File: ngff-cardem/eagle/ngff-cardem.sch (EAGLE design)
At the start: 143 parts, among them IC201 CB3Q3244PW, IC202 CB3Q3244PW, IC203 IP4234CZ6, IC204 FPF2109, IC205 FPF2109, IC301 TPS22958N-DGN, IC302 TPS22958N-DGK, J301 PJ-002BH-SMT-TR, M2 MENTOR_12701001, M3 MENTOR_12701001, Q201 12MHz, T101 BC847, T102 BC847, U201 IP4234CZ6, U202 AT91SAM3S-AU, U301 MIC5366-1.8YC5, X101 PINHD-2X3-SP, X102 ZX360D-B-10P(30), X201 MINI-USB-SHIELD-UX60-MB-5ST, X202 2.54mm, X203 JACK2.5_SJ-2523, X301 171826-4-RA

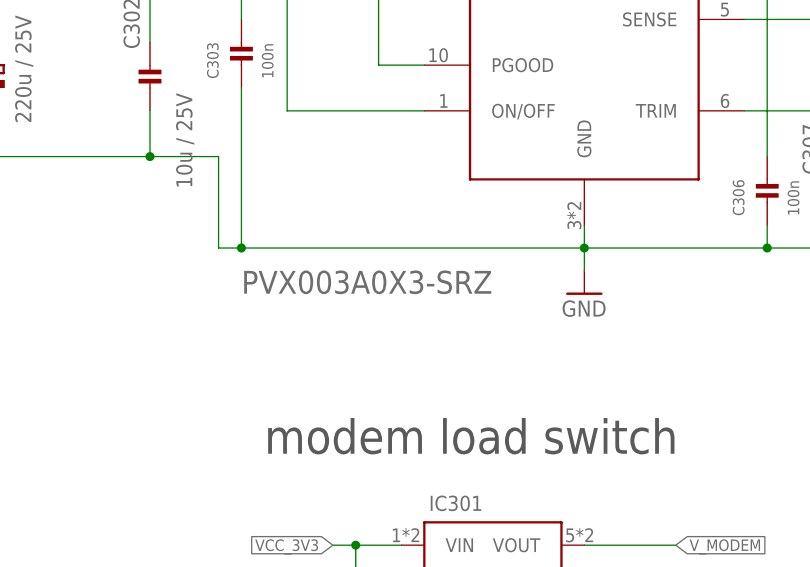
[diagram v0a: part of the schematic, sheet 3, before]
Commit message: ngff-cardem: make DCDC301 default to Murata OKL-T/3-W12P-C
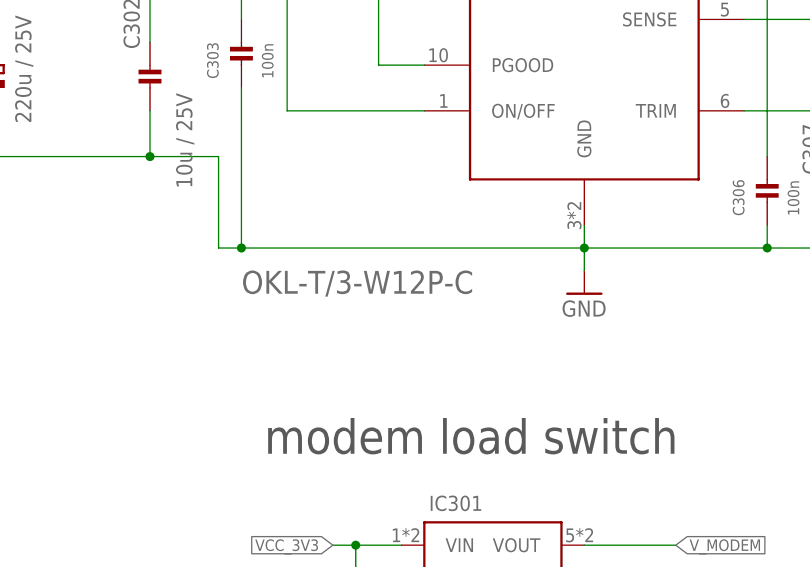
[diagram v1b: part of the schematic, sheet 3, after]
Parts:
- DCDC301: value PVX003A0X3-SRZ -> OKL-T/3-W12P-C; DESCRIPTION DC DC CONVERTER 0.6-5.5V 16.5W -> DC DC CONVERTER 0.591-5.5V 15W; LINK https://www.digikey.de/product-detail/de/abb-power-electron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 -> https://www.digikey.de/product-detail/de/murata-power-solut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; MANUFACTURER ABB Power Electronics Inc. -> Murata Power Solutions Inc.; MANUFACTURERPARTNUMBER PVX003A0X3-SRZ -> OKL-T/3-W12P-C; SOURCEPARTNUMBER 555-1264-1-ND -> 811-2709-1-ND
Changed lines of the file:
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@@
 <attribute name="SOURCEPARTNUMBER" value="732-6126-1-ND"/>
 </part>
-<part name="DCDC301" library="DC-DC_CONVERTER" deviceset="DCDC-GE-PVX" device="-ALL" value="PVX003A0X3-SRZ">
+<part name="DCDC301" library="DC-DC_CONVERTER" deviceset="DCDC-GE-PVX" device="-ALL" value="OKL-T/3-W12P-C">
 <attribute name="CLASS" value="DC/DC CONVERTER"/>
-<attribute name="DESCRIPTION" value="DC DC CONVERTER 0.6-5.5V 16.5W"/>
-<attribute name="LINK" value="https://www.digikey.de/product-detail/de/abb-power-electronics-inc/PVX003A0X3-SRZ/555-1264-1-ND"/>
-<attribute name="MANUFACTURER" value="ABB Power Electronics Inc."/>
-<attribute name="MANUFACTURERPARTNUMBER" value="PVX003A0X3-SRZ"/>
+<attribute name="DESCRIPTION" value="DC DC CONVERTER 0.591-5.5V 15W"/>
+<attribute name="LINK" value="https://www.digikey.de/product-detail/de/murata-power-solutions-inc/OKL-T-3-W12P-C/811-2709-1-ND"/>
+<attribute name="MANUFACTURER" value="Murata Power Solutions Inc."/>
+<attribute name="MANUFACTURERPARTNUMBER" value="OKL-T/3-W12P-C"/>
 <attribute name="POPULATED" value="TRUE"/>
 <attribute name="ROHSCERTIFICATE" value="RoHS-konform"/>
 <attribute name="SOURCE" value="DIGIKEY"/>
-<attribute name="SOURCEPARTNUMBER" value="555-1264-1-ND"/>
+<attribute name="SOURCEPARTNUMBER" value="811-2709-1-ND"/>
 </part>
 <part name="R304" library="rc-sysmocom" deviceset="RESISTOR" device="_0603" value="100k">
@@
 <attribute name="NAME" x="273.558" y="252.73" size="2.54" layer="95"/>
 <attribute name="VALUE" x="243.84" y="213.36" size="2.54" layer="96"/>
-<attribute name="DESCRIPTION" x="281.94" y="238.76" size="1.27" layer="96" display="off"/>
-<attribute name="MANUFACTURER" x="281.94" y="238.76" size="1.27" layer="96" display="off"/>
-<attribute name="MANUFACTURERPARTNUMBER" x="281.94" y="238.76" size="1.27" layer="96" display="off"/>
-<attribute name="SOURCE" x="281.94" y="238.76" size="1.27" layer="96" display="off"/>
-<attribute name="SOURCEPARTNUMBER" x="281.94" y="238.76" size="1.27" layer="96" display="off"/>
-<attribute name="ROHSCERTIFICATE" x="281.94" y="238.76" size="1.27" layer="96" display="off"/>
-<attribute name="POPULATED" x="281.94" y="238.76" size="1.27" layer="96" display="off"/>
-<attribute name="CLASS" x="281.94" y="238.76" size="1.27" layer="96" display="off"/>
-<attribute name="LINK" x="281.94" y="238.76" size="1.27" layer="96" display="off"/>
+<attribute name="DESCRIPTION" x="281.94" y="238.76" size="1.778" layer="96" display="off"/>
+<attribute name="MANUFACTURER" x="281.94" y="238.76" size="1.778" layer="96" display="off"/>
+<attribute name="MANUFACTURERPARTNUMBER" x="281.94" y="238.76" size="1.778" layer="96" display="off"/>
+<attribute name="SOURCE" x="281.94" y="238.76" size="1.778" layer="96" display="off"/>
+<attribute name="SOURCEPARTNUMBER" x="281.94" y="238.76" size="1.778" layer="96" display="off"/>
+<attribute name="ROHSCERTIFICATE" x="281.94" y="238.76" size="1.778" layer="96" display="off"/>
+<attribute name="POPULATED" x="281.94" y="238.76" size="1.778" layer="96" display="off"/>
+<attribute name="CLASS" x="281.94" y="238.76" size="1.778" layer="96" display="off"/>
+<attribute name="LINK" x="281.94" y="238.76" size="1.778" layer="96" display="off"/>
 </instance>
 <instance part="R304" gate="G$1" x="264.16" y="256.54" smashed="yes" rot="R180">

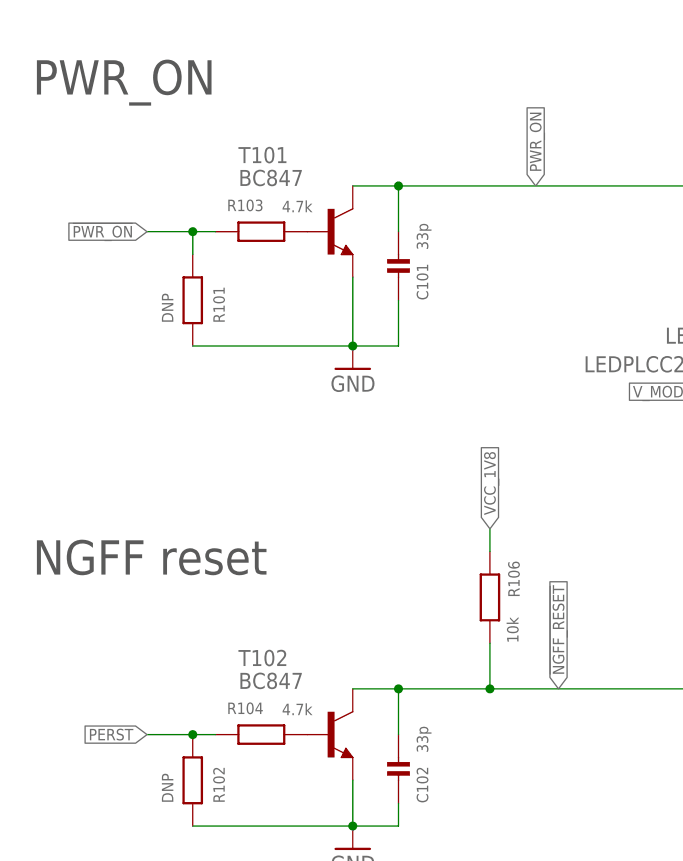
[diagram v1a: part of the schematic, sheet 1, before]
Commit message: ngff-cardem: exchange two BJT to available types (BC850)
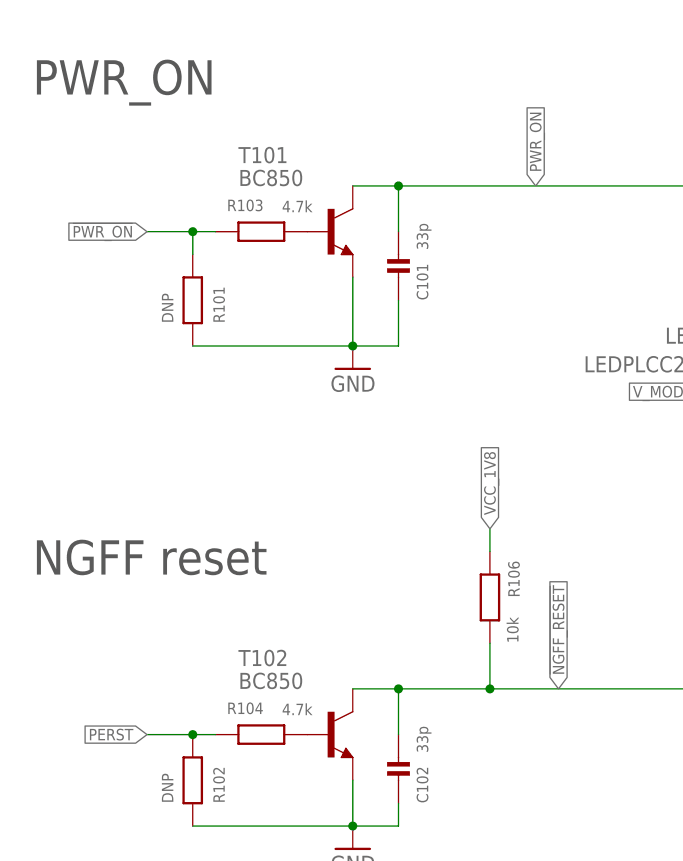
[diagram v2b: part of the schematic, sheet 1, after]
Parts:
- T101, T102: value BC847 -> BC850; DESCRIPTION TRANS NPN 45V 0.1A SOT23 -> TRANS NPN 45V 100MA TO236AB; LINK https://www.digikey.de/product-detail/de/nexperia-usa-inc/BC847C,215/1727-2924-1-ND -> https://www.digikey.de/product-detail/de/nexperia-usa-inc/BC850C-235/1727-6194-1-ND/; MANUFACTURERPARTNUMBER BC847C,215 -> BC850C,235; SOURCEPARTNUMBER 1727-2924-1-ND -> 1727-6194-1-ND
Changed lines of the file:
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@@
 <attribute name="SOURCEPARTNUMBER" value="A121523CT-ND"/>
 </part>
-<part name="T101" library="transistor" deviceset="*-NPN-" device="SOT23-BEC" technology="BC847C" value="BC847">
+<part name="T101" library="transistor" deviceset="*-NPN-" device="SOT23-BEC" technology="BC847C" value="BC850">
 <attribute name="CLASS" value="TRANSISTOR"/>
-<attribute name="DESCRIPTION" value="TRANS NPN 45V 0.1A SOT23"/>
-<attribute name="LINK" value="https://www.digikey.de/product-detail/de/nexperia-usa-inc/BC847C,215/1727-2924-1-ND"/>
+<attribute name="DESCRIPTION" value="TRANS NPN 45V 100MA TO236AB"/>
+<attribute name="LINK" value="https://www.digikey.de/product-detail/de/nexperia-usa-inc/BC850C-235/1727-6194-1-ND/"/>
 <attribute name="MANUFACTURER" value="Nexperia USA Inc."/>
-<attribute name="MANUFACTURERPARTNUMBER" value="BC847C,215"/>
-<attribute name="POPULATED" value="TRUE"/>
-<attribute name="ROHSCERTIFICATE" value="RoHS3-konform"/>
-<attribute name="SOURCE" value="DIGIKEY"/>
-<attribute name="SOURCEPARTNUMBER" value="1727-2924-1-ND"/>
+<attribute name="MANUFACTURERPARTNUMBER" value="BC850C,235"/>
+<attribute name="POPULATED" value="TRUE"/>
+<attribute name="ROHSCERTIFICATE" value="RoHS3-konform"/>
+<attribute name="SOURCE" value="DIGIKEY"/>
+<attribute name="SOURCEPARTNUMBER" value="1727-6194-1-ND"/>
 </part>
 <part name="GND47" library="supply1" deviceset="GND" device=""/>
@@
 <attribute name="SOURCEPARTNUMBER" value="A129611CT-ND"/>
 </part>
-<part name="T102" library="transistor" deviceset="*-NPN-" device="SOT23-BEC" technology="BC847C" value="BC847">
+<part name="T102" library="transistor" deviceset="*-NPN-" device="SOT23-BEC" technology="BC847C" value="BC850">
 <attribute name="CLASS" value="TRANSISTOR"/>
-<attribute name="DESCRIPTION" value="TRANS NPN 45V 0.1A SOT23"/>
-<attribute name="LINK" value="https://www.digikey.de/product-detail/de/nexperia-usa-inc/BC847C,215/1727-2924-1-ND"/>
+<attribute name="DESCRIPTION" value="TRANS NPN 45V 100MA TO236AB"/>
+<attribute name="LINK" value="https://www.digikey.de/product-detail/de/nexperia-usa-inc/BC850C-235/1727-6194-1-ND/"/>
 <attribute name="MANUFACTURER" value="Nexperia USA Inc."/>
-<attribute name="MANUFACTURERPARTNUMBER" value="BC847C,215"/>
-<attribute name="POPULATED" value="TRUE"/>
-<attribute name="ROHSCERTIFICATE" value="RoHS3-konform"/>
-<attribute name="SOURCE" value="DIGIKEY"/>
-<attribute name="SOURCEPARTNUMBER" value="1727-2924-1-ND"/>
+<attribute name="MANUFACTURERPARTNUMBER" value="BC850C,235"/>
+<attribute name="POPULATED" value="TRUE"/>
+<attribute name="ROHSCERTIFICATE" value="RoHS3-konform"/>
+<attribute name="SOURCE" value="DIGIKEY"/>
+<attribute name="SOURCEPARTNUMBER" value="1727-6194-1-ND"/>
 </part>
 <part name="GND16" library="supply1" deviceset="GND" device=""/>
@@
 </instance>
 <instance part="T101" gate="G$1" x="60.96" y="195.58">
-<attribute name="DESCRIPTION" x="60.96" y="195.58" size="1.778" layer="96" rot="MR0" display="off"/>
-<attribute name="MANUFACTURER" x="60.96" y="195.58" size="1.778" layer="96" rot="MR0" display="off"/>
-<attribute name="MANUFACTURERPARTNUMBER" x="60.96" y="195.58" size="1.778" layer="96" rot="MR0" display="off"/>
-<attribute name="SOURCE" x="60.96" y="195.58" size="1.778" layer="96" rot="MR0" display="off"/>
-<attribute name="SOURCEPARTNUMBER" x="60.96" y="195.58" size="1.778" layer="96" rot="MR0" display="off"/>
-<attribute name="ROHSCERTIFICATE" x="60.96" y="195.58" size="1.778" layer="96" rot="MR0" display="off"/>
-<attribute name="POPULATED" x="60.96" y="195.58" size="1.778" layer="96" rot="MR0" display="off"/>
-<attribute name="CLASS" x="60.96" y="195.58" size="1.778" layer="96" rot="MR0" display="off"/>
-<attribute name="LINK" x="60.96" y="195.58" size="1.778" layer="96" rot="MR0" display="off"/>
+<attribute name="DESCRIPTION" x="60.96" y="195.58" size="1.778" layer="96" display="off"/>
+<attribute name="MANUFACTURER" x="60.96" y="195.58" size="1.778" layer="96" display="off"/>
+<attribute name="MANUFACTURERPARTNUMBER" x="60.96" y="195.58" size="1.778" layer="96" display="off"/>
+<attribute name="SOURCE" x="60.96" y="195.58" size="1.778" layer="96" display="off"/>
+<attribute name="SOURCEPARTNUMBER" x="60.96" y="195.58" size="1.778" layer="96" display="off"/>
+<attribute name="ROHSCERTIFICATE" x="60.96" y="195.58" size="1.778" layer="96" display="off"/>
+<attribute name="POPULATED" x="60.96" y="195.58" size="1.778" layer="96" display="off"/>
+<attribute name="CLASS" x="60.96" y="195.58" size="1.778" layer="96" display="off"/>
+<attribute name="LINK" x="60.96" y="195.58" size="1.778" layer="96" display="off"/>
 </instance>
 <instance part="GND47" gate="1" x="63.5" y="180.34" rot="MR0"/>
@@
 </instance>
 <instance part="T102" gate="G$1" x="60.96" y="139.7">
-<attribute name="DESCRIPTION" x="60.96" y="139.7" size="1.778" layer="96" rot="MR0" display="off"/>
-<attribute name="MANUFACTURER" x="60.96" y="139.7" size="1.778" layer="96" rot="MR0" display="off"/>
-<attribute name="MANUFACTURERPARTNUMBER" x="60.96" y="139.7" size="1.778" layer="96" rot="MR0" display="off"/>
-<attribute name="SOURCE" x="60.96" y="139.7" size="1.778" layer="96" rot="MR0" display="off"/>
-<attribute name="SOURCEPARTNUMBER" x="60.96" y="139.7" size="1.778" layer="96" rot="MR0" display="off"/>
-<attribute name="ROHSCERTIFICATE" x="60.96" y="139.7" size="1.778" layer="96" rot="MR0" display="off"/>
-<attribute name="POPULATED" x="60.96" y="139.7" size="1.778" layer="96" rot="MR0" display="off"/>
-<attribute name="CLASS" x="60.96" y="139.7" size="1.778" layer="96" rot="MR0" display="off"/>
-<attribute name="LINK" x="60.96" y="139.7" size="1.778" layer="96" rot="MR0" display="off"/>
+<attribute name="DESCRIPTION" x="60.96" y="139.7" size="1.778" layer="96" display="off"/>
+<attribute name="MANUFACTURER" x="60.96" y="139.7" size="1.778" layer="96" display="off"/>
+<attribute name="MANUFACTURERPARTNUMBER" x="60.96" y="139.7" size="1.778" layer="96" display="off"/>
+<attribute name="SOURCE" x="60.96" y="139.7" size="1.778" layer="96" display="off"/>
+<attribute name="SOURCEPARTNUMBER" x="60.96" y="139.7" size="1.778" layer="96" display="off"/>
+<attribute name="ROHSCERTIFICATE" x="60.96" y="139.7" size="1.778" layer="96" display="off"/>
+<attribute name="POPULATED" x="60.96" y="139.7" size="1.778" layer="96" display="off"/>
+<attribute name="CLASS" x="60.96" y="139.7" size="1.778" layer="96" display="off"/>
+<attribute name="LINK" x="60.96" y="139.7" size="1.778" layer="96" display="off"/>
 </instance>
 <instance part="GND16" gate="1" x="63.5" y="127" rot="MR0"/>

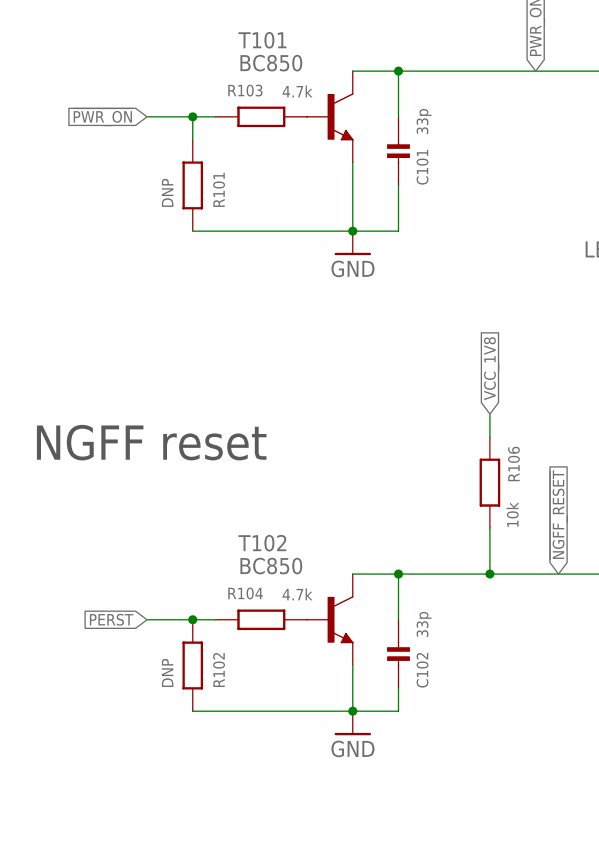
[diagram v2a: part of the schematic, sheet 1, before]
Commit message: ngff-cardem: populate R102 to uncond' release /NGFF_RESET (solves SYS#5531)
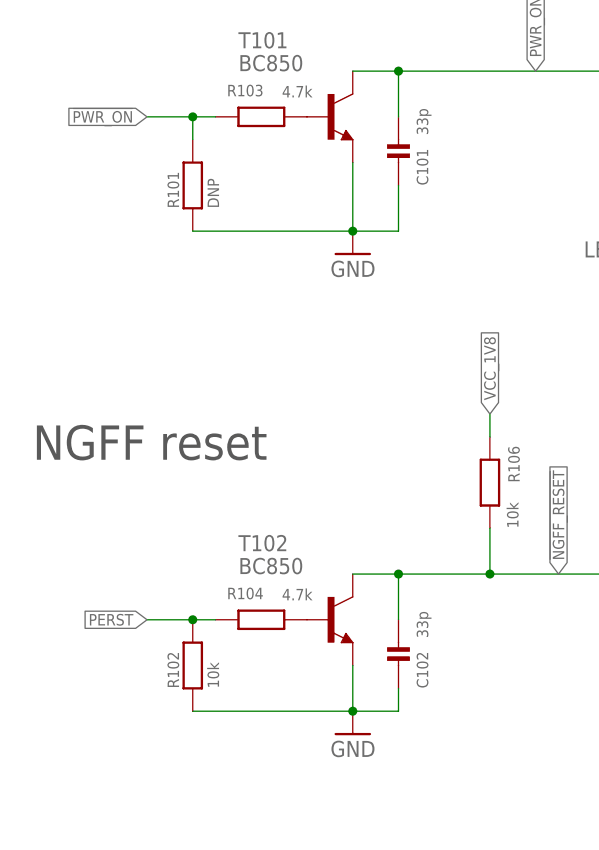
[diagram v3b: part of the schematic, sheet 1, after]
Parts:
- R102: value DNP -> 10k; DESCRIPTION NO DESCRIPTION -> RES SMD 10K OHM 1%% 1/10W 0603; LINK UNKNOWN LINK -> https://www.digikey.de/product-detail/de/te-connectivity-pa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; MANUFACTURER UNKNOWN MANUFACTURER -> TE Connectivity Passive Product; MANUFACTURERPARTNUMBER UNKNOWN MANUFACTURER PART NUMBER -> CRG0603F10K/10; POPULATED FALSE -> TRUE; ROHSCERTIFICATE UNKNOWN ROHS CERTIFICATE -> RoHS3-konform; SOURCE UNKNOWN SOURCE -> DIGIKEY; SOURCEPARTNUMBER UNKNOWN SOURCE PART NUMBER -> A121523CT-ND
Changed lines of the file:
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@@
 <attribute name="SOURCEPARTNUMBER" value="1276-1272-1-ND"/>
 </part>
-<part name="R102" library="rc-sysmocom" deviceset="RESISTOR" device="_0603" value="DNP">
+<part name="R102" library="rc-sysmocom" deviceset="RESISTOR" device="_0603" value="10k">
 <attribute name="CLASS" value="RESISTOR"/>
-<attribute name="DESCRIPTION" value="NO DESCRIPTION"/>
-<attribute name="LINK" value="UNKNOWN LINK"/>
-<attribute name="MANUFACTURER" value="UNKNOWN MANUFACTURER"/>
-<attribute name="MANUFACTURERPARTNUMBER" value="UNKNOWN MANUFACTURER PART NUMBER"/>
-<attribute name="POPULATED" value="FALSE"/>
-<attribute name="ROHSCERTIFICATE" value="UNKNOWN ROHS CERTIFICATE"/>
-<attribute name="SOURCE" value="UNKNOWN SOURCE"/>
-<attribute name="SOURCEPARTNUMBER" value="UNKNOWN SOURCE PART NUMBER"/>
+<attribute name="DESCRIPTION" value="RES SMD 10K OHM 1%% 1/10W 0603"/>
+<attribute name="LINK" value="https://www.digikey.de/product-detail/de/te-connectivity-passive-product/CRG0603F10K-10/A121523CT-ND/"/>
+<attribute name="MANUFACTURER" value="TE Connectivity Passive Product"/>
+<attribute name="MANUFACTURERPARTNUMBER" value="CRG0603F10K/10"/>
+<attribute name="POPULATED" value="TRUE"/>
+<attribute name="ROHSCERTIFICATE" value="RoHS3-konform"/>
+<attribute name="SOURCE" value="DIGIKEY"/>
+<attribute name="SOURCEPARTNUMBER" value="A121523CT-ND"/>
 </part>
 <part name="R104" library="rc-sysmocom" deviceset="RESISTOR" device="_0603" value="4.7k">
@@
 </instance>
 <instance part="R101" gate="G$1" x="45.72" y="187.96" smashed="yes" rot="MR270">
-<attribute name="NAME" x="48.006" y="185.42" size="1.27" layer="95" rot="MR90"/>
-<attribute name="VALUE" x="42.291" y="185.42" size="1.27" layer="96" rot="MR90"/>
+<attribute name="NAME" x="42.926" y="185.42" size="1.27" layer="95" rot="MR90"/>
+<attribute name="VALUE" x="47.371" y="185.42" size="1.27" layer="96" rot="MR90"/>
 <attribute name="DESCRIPTION" x="45.72" y="187.96" size="1.778" layer="96" display="off"/>
 <attribute name="MANUFACTURER" x="45.72" y="187.96" size="1.778" layer="96" display="off"/>
@@
 </instance>
 <instance part="R102" gate="G$1" x="45.72" y="134.62" smashed="yes" rot="MR270">
-<attribute name="NAME" x="48.006" y="132.08" size="1.27" layer="95" rot="MR90"/>
-<attribute name="VALUE" x="42.291" y="132.08" size="1.27" layer="96" rot="MR90"/>
+<attribute name="NAME" x="42.926" y="132.08" size="1.27" layer="95" rot="MR90"/>
+<attribute name="VALUE" x="47.371" y="132.08" size="1.27" layer="96" rot="MR90"/>
 <attribute name="DESCRIPTION" x="45.72" y="134.62" size="1.778" layer="96" display="off"/>
 <attribute name="MANUFACTURER" x="45.72" y="134.62" size="1.778" layer="96" display="off"/>
